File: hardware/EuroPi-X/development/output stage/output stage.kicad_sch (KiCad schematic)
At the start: 27 parts, among them J1 Conn_01x06_Pin, J2 Conn_01x06_Pin, U1 TL074

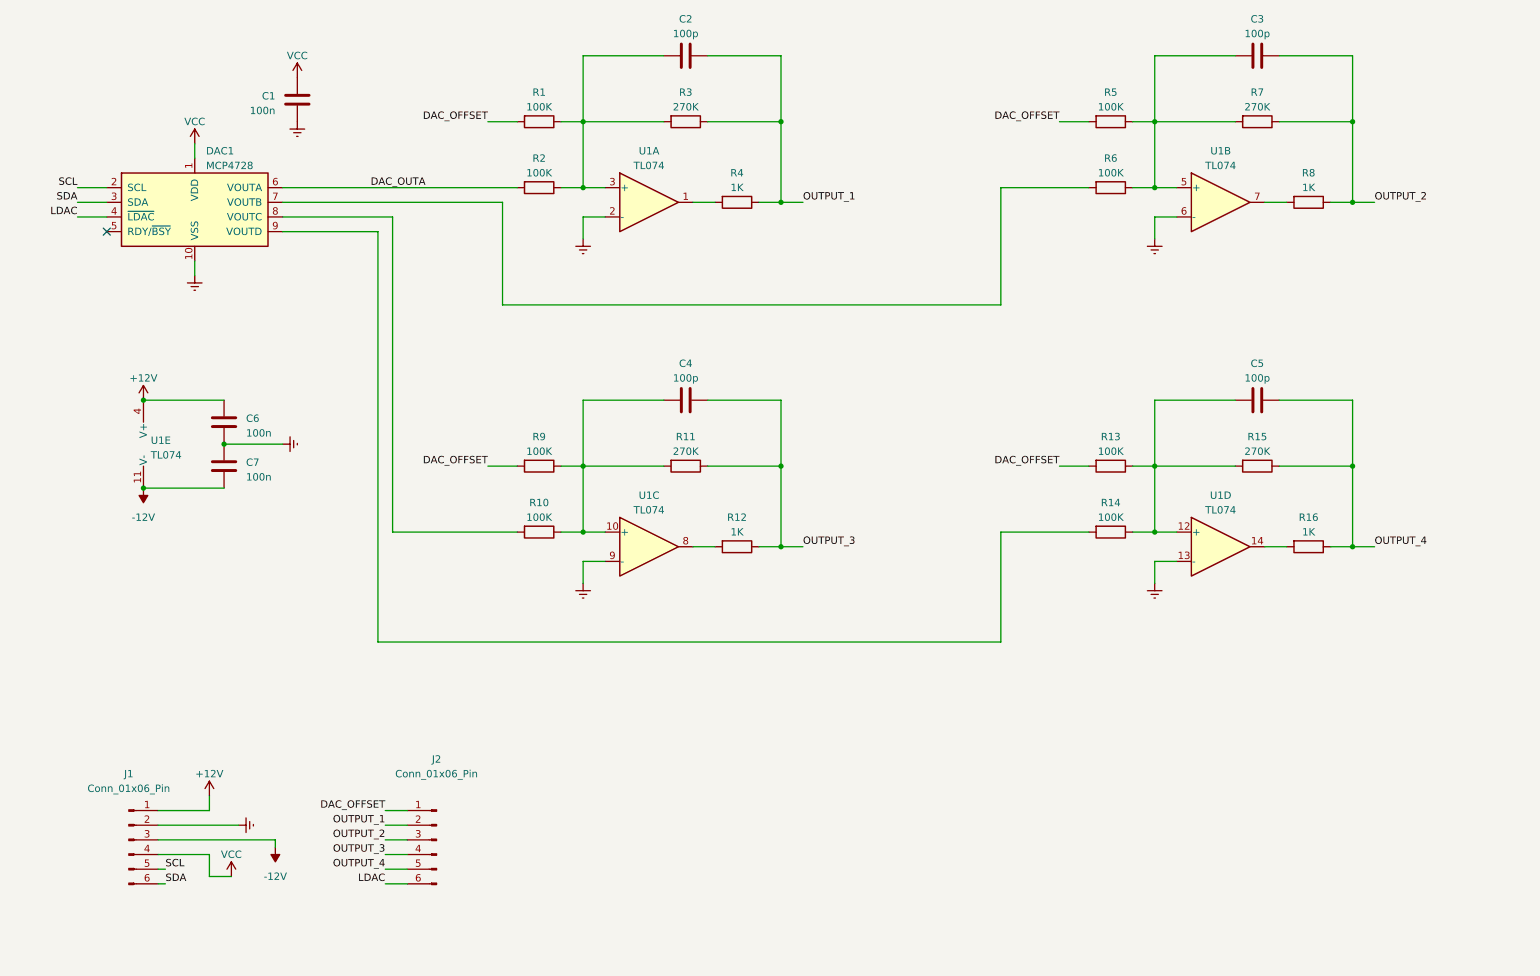
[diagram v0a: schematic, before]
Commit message: save output stage
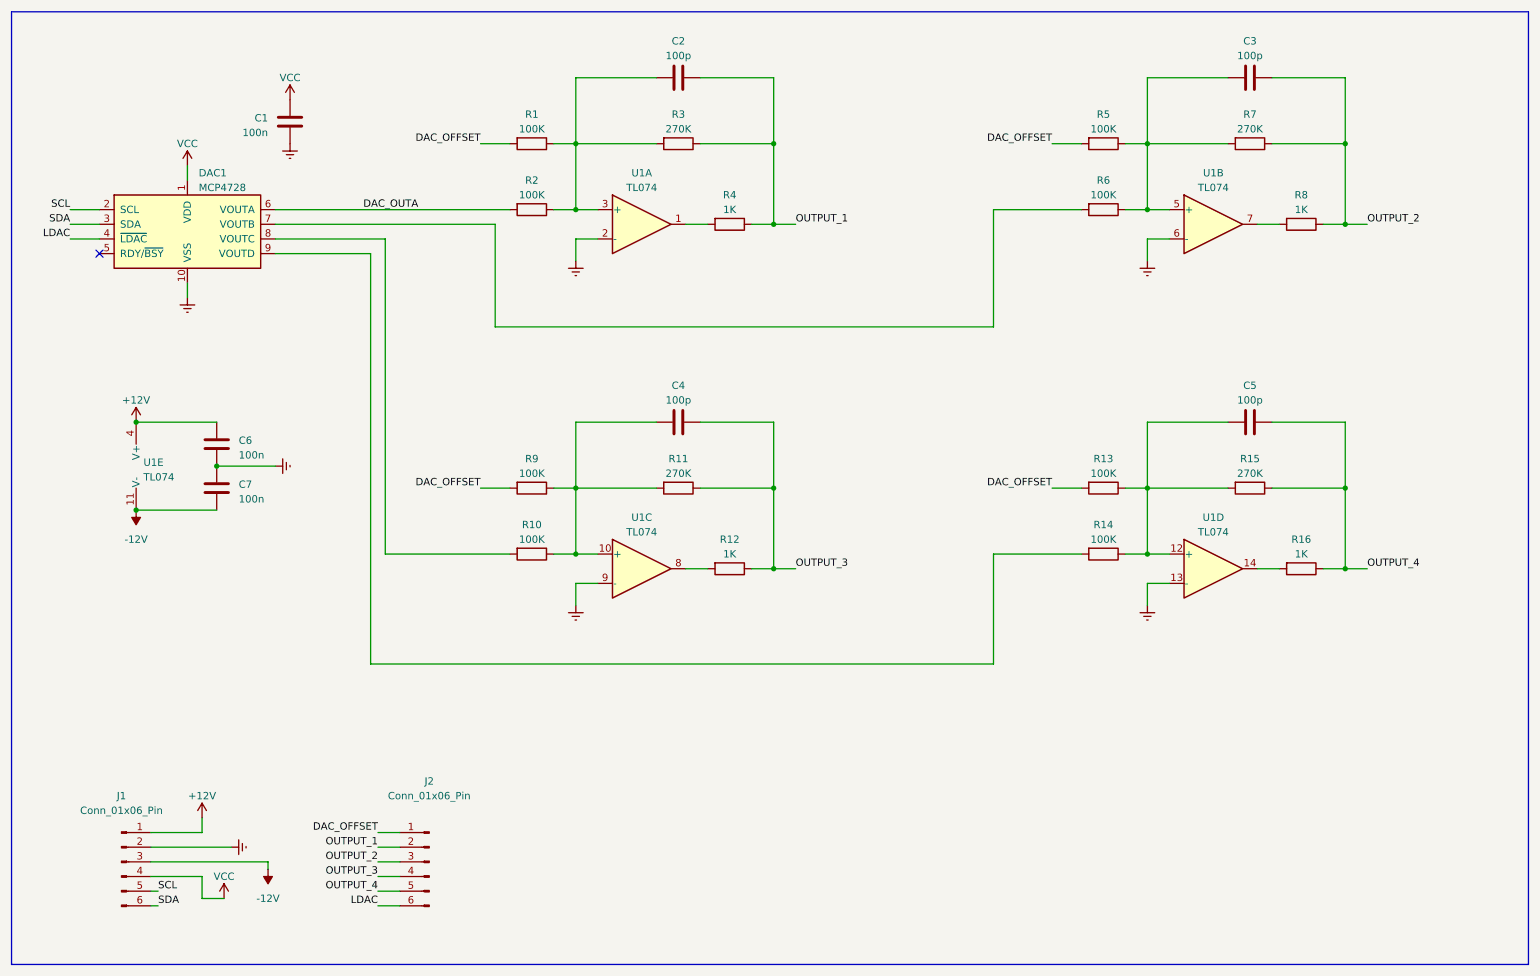
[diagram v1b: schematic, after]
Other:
- moved on the sheet: C1, C2, C3, C4, C5, C6, C7, DAC1, J1, J2, R1, R10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

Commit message: save
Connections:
- net OUTPUT_1: no longer C2.2
- net OUTPUT_2: no longer C3.2
- net OUTPUT_3: no longer C4.2
- net OUTPUT_4: no longer C5.2
- net at R4.2, U1.1: now also C2.2
- net at R8.2, U1.7: now also C3.2
- net at R16.2, U1.14: now also C5.2
- net at R12.2, U1.8: now also C4.2
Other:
- moved on the sheet: C2, C3, C4, C5, R11, R15, R3, R7
